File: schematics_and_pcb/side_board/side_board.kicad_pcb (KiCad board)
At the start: 2 copper layers, 13.9 x 33.1 mm, 9 parts, among them J1 Conn_01x04_Male

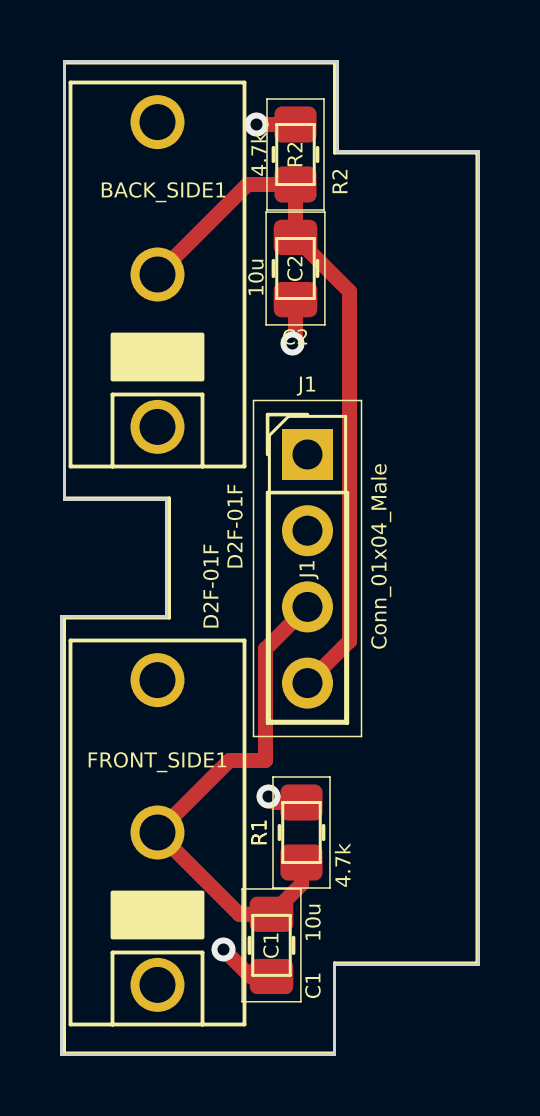
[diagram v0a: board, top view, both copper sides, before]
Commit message: fixed some of the routing
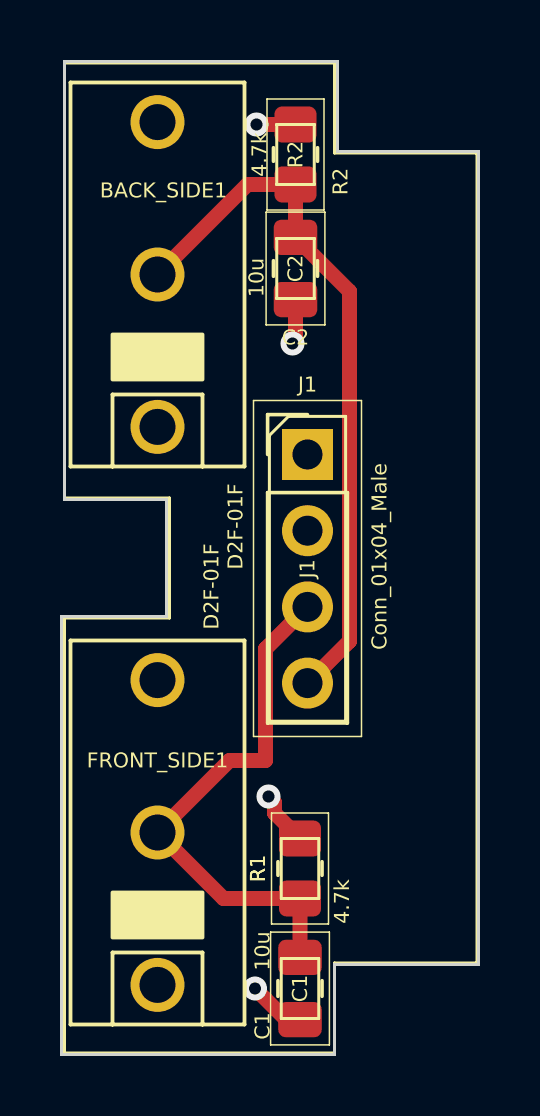
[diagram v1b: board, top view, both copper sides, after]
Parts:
- moved C1 1.72 mm to (43.8, 64.0)
- moved R1 1.20 mm to (43.8, 60.0)
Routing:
- net GND: track 5.96 -> 6.57 mm
- net FRONT_STATE: track 17.4 -> 17.9 mm
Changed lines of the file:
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@@
   )
   (footprint "Resistor_SMD:R_0805_2012Metric_Pad1.20x1.40mm_HandSolder" (layer "F.Cu")
-    (at 43.8 58.8 -90)
+    (at 43.75 60 -90)
     (descr "Resistor SMD 0805 (2012 Metric), square (rectangular) end terminal, IPC_7351 nominal with elongated pad for handsoldering. (Body size source: IPC-SM-782 page 72, https://www.pcb-3d.com/wordpress/wp-content/uploads/ipc-sm-782a_amendment_1_and_2.pdf), generated with kicad-footprint-generator")
     (tags "resistor handsolder")
@@
   )
   (footprint "Capacitor_SMD:C_0805_2012Metric_Pad1.18x1.45mm_HandSolder" (layer "F.Cu")
-    (at 42.8 62.5625 90)
+    (at 43.75 64 90)
     (descr "Capacitor SMD 0805 (2012 Metric), square (rectangular) end terminal, IPC_7351 nominal with elongated pad for handsoldering. (Body size source: IPC-SM-782 page 76, https://www.pcb-3d.com/wordpress/wp-content/uploads/ipc-sm-782a_amendment_1_and_2.pdf, https://docs.google.com/spreadsheets/d/1BsfQQcO9C6DZCsRaXUlFlo91Tg2WpOkGARC1WS5S8t0/edit?usp=sharing), generated with kicad-footprint-generator")
     (tags "capacitor handsolder")
@@
     (property "Sheetname" "")
     (attr smd)
-    (fp_text reference "C1" (at -1.3375 1.4 90) (layer "F.SilkS")
-      (effects (font (size 0.5 0.5) (thickness 0.1)))
-    )
-    (fp_text value "10u" (at 0.7625 1.4 90) (layer "F.SilkS")
+    (fp_text reference "C1" (at -1.25 -1.25 90) (layer "F.SilkS")
+      (effects (font (size 0.5 0.5) (thickness 0.1)))
+    )
+    (fp_text value "10u" (at 1.25 -1.25 90) (layer "F.SilkS")
       (effects (font (size 0.5 0.5) (thickness 0.1)))
     )
@@
     (effects (font (size 0.5 0.5) (thickness 0.1)) (justify mirror))
   )
-  (segment (start 43.8 57.8) (end 42.9 57.8) (width 0.5) (layer "F.Cu") (net 1))
+  (segment (start 43.75 59) (end 42.9 58.15) (width 0.5) (layer "F.Cu") (net 1))
+  (segment (start 42.9 58.15) (end 42.9 57.8) (width 0.5) (layer "F.Cu") (net 1))
+  (segment (start 43.75 65.0375) (end 43.2875 65.0375) (width 0.5) (layer "F.Cu") (net 1))
   (segment (start 43.6 35.2) (end 42.3 35.2) (width 0.5) (layer "F.Cu") (net 1))
-  (segment (start 42.1 63.6) (end 41.2 62.7) (width 0.5) (layer "F.Cu") (net 1))
+  (segment (start 43.2875 65.0375) (end 42.25 64) (width 0.5) (layer "F.Cu") (net 1))
   (segment (start 43.6 41.0375) (end 43.6 42.4) (width 0.5) (layer "F.Cu") (net 1))
   (segment (start 43.6 42.4) (end 43.5 42.5) (width 0.5) (layer "F.Cu") (net 1))
-  (segment (start 42.8 63.6) (end 42.1 63.6) (width 0.5) (layer "F.Cu") (net 1))
   (segment (start 42.9 57.8) (end 42.7 57.6) (width 0.5) (layer "F.Cu") (net 1))
-  (via (at 41.2 62.7) (size 0.8) (drill 0.4) (layers "F.Cu" "B.Cu") (net 1))
+  (via (at 42.25 64) (size 0.8) (drill 0.4) (layers "F.Cu" "B.Cu") (net 1))
   (via (at 42.7 57.6) (size 0.8) (drill 0.4) (layers "F.Cu" "B.Cu") (net 1))
   (via (at 42.3 35.2) (size 0.8) (drill 0.4) (layers "F.Cu" "B.Cu") (net 1))
   (via (at 43.5 42.5) (size 0.8) (drill 0.4) (layers "F.Cu" "B.Cu") (net 1))
-  (segment (start 41.725 61.525) (end 39 58.8) (width 0.5) (layer "F.Cu") (net 2))
   (segment (start 42.6 56.4) (end 42.6 52.68) (width 0.5) (layer "F.Cu") (net 2))
+  (segment (start 43.75 61) (end 41.2 61) (width 0.5) (layer "F.Cu") (net 2))
   (segment (start 41.4 56.4) (end 42.6 56.4) (width 0.5) (layer "F.Cu") (net 2))
-  (segment (start 43.8 59.8) (end 43.8 60.525) (width 0.5) (layer "F.Cu") (net 2))
   (segment (start 39 58.8) (end 41.4 56.4) (width 0.5) (layer "F.Cu") (net 2))
+  (segment (start 41.2 61) (end 39 58.8) (width 0.5) (layer "F.Cu") (net 2))
   (segment (start 42.6 52.68) (end 44 51.28) (width 0.5) (layer "F.Cu") (net 2))
-  (segment (start 42.8 61.525) (end 41.725 61.525) (width 0.5) (layer "F.Cu") (net 2))
-  (segment (start 43.8 60.525) (end 42.8 61.525) (width 0.5) (layer "F.Cu") (net 2))
+  (segment (start 43.75 62.9625) (end 43.75 61) (width 0.5) (layer "F.Cu") (net 2))
   (segment (start 43.6 38.9625) (end 45.4 40.7625) (width 0.5) (layer "F.Cu") (net 3))
   (segment (start 39 40.2) (end 42 37.2) (width 0.5) (layer "F.Cu") (net 3))
